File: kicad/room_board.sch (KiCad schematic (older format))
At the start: 22 parts, among them K1 CONN_3, U1 MSP430G2553IN20, U2 7805, U3 DHT

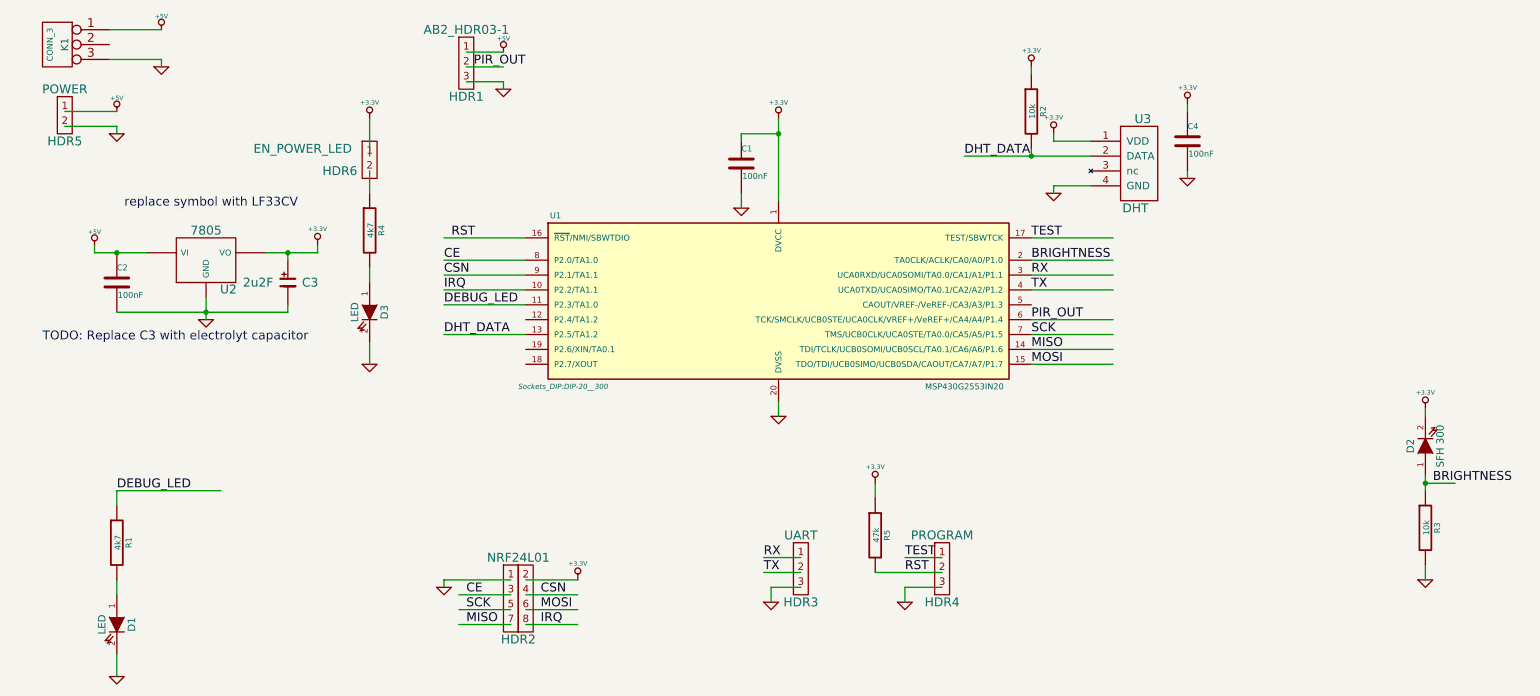
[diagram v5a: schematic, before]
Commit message: update schematic/layout
- replace LM7805 symbol with LM33CV in schematic and layout
- add 3.3V power connector in schematic and layout
- replace 3pin uart with 6pin. only in schematic not done yet in layout
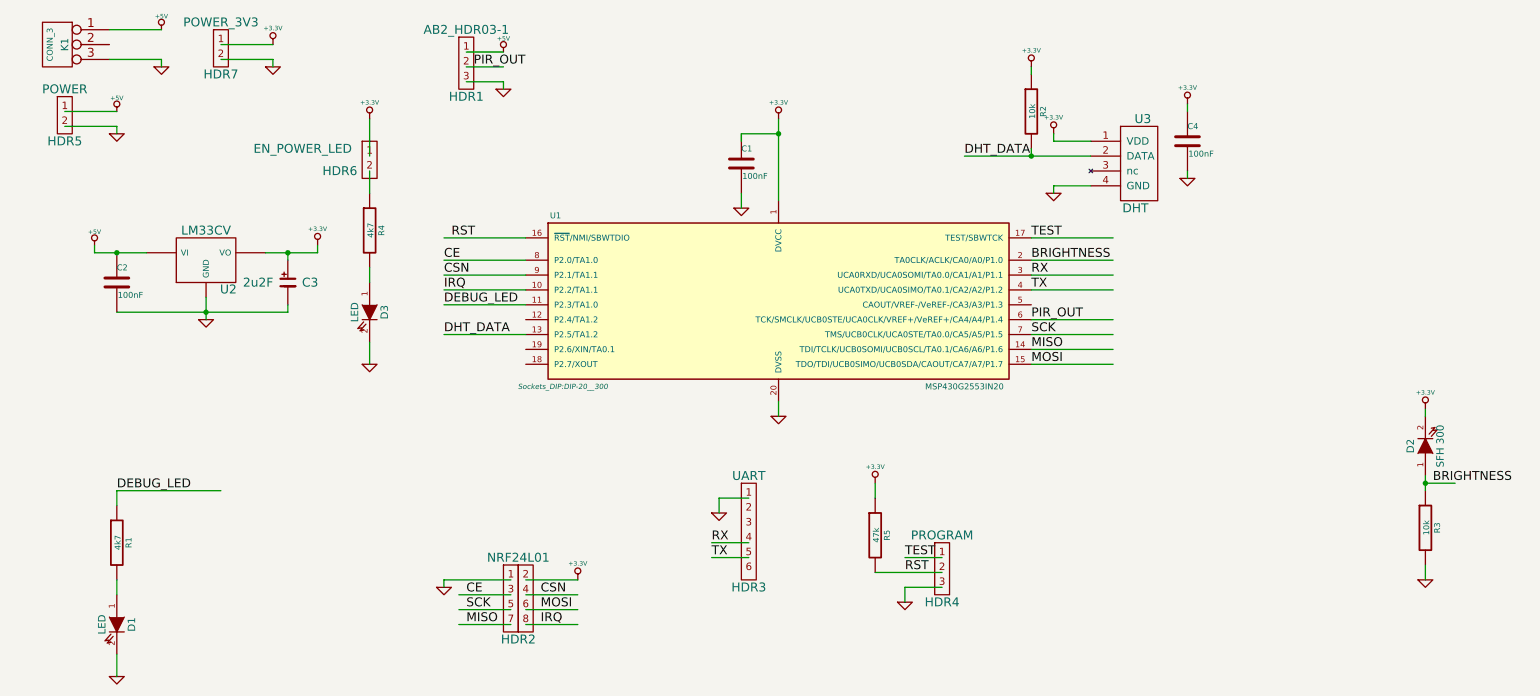
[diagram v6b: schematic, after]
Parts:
- removed HDR3: UART, ab2_header:AB2_HDR_M03-1V, symbol AB2_HDR03-1
- removed U2: 7805, Discret:LM78XXV, symbol 7805
- added HDR3: UART, ab2_header:AB2_HDR_M06-1H-L, symbol AB2_HDR06-1
- added HDR7: POWER_3V3, ab2_header:AB2_HDR_M02-1V, symbol AB2_HDR02-1
- added U2: LM33CV, Discret:LM78XXV, symbol LM33CV
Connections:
- wire segments 76 -> 79
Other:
- note removed: "TODO: Replace C3 with electrolyt capacitor"
- note removed: "replace symbol with LF33CV"
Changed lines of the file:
@@
 LIBS:ab2_usb
 LIBS:ab2_xtal
+LIBS:fr_regulator
 LIBS:room_board-cache
 EELAYER 25 0
@@
 $EndComp
 $Comp
-L 7805 U2
-U 1 1 541A1855
-P 1750 2250
-F 0 "U2" H 1900 2054 60  0000 C CNN
-F 1 "7805" H 1750 2450 60  0000 C CNN
-F 2 "Discret:LM78XXV" H 1750 2250 60  0001 C CNN
-F 3 "" H 1750 2250 60  0000 C CNN
-	1    1750 2250
-	1    0    0    -1
-$EndComp
-$Comp
 L C C2
 U 1 1 541A1A82
@@
 	1    0    0    -1
 $EndComp
-Text Notes 1200 1900 0    60   ~ 0
-replace symbol with LF33CV
 $Comp
 L AB2_HDR03-1 HDR1
@@
 	3800 4400 3350 4400
 $Comp
-L AB2_HDR03-1 HDR3
-U 1 1 54265497
-P 5750 4250
-F 0 "HDR3" H 5750 3950 60  0000 C CNN
-F 1 "UART" H 5750 4400 60  0000 C CNN
-F 2 "ab2_header:AB2_HDR_M03-1V" H 5750 4250 60  0001 C CNN
-F 3 "" H 5750 4250 60  0000 C CNN
-	1    5750 4250
-	1    0    0    -1
-$EndComp
-$Comp
 L AB2_HDR03-1 HDR4
 U 1 1 542654DE
@@
 	1    0    0    -1
 $EndComp
-Text Label 5500 4250 0    60   ~ 0
+Text Label 5150 4150 0    60   ~ 0
 RX
-Text Label 5500 4350 0    60   ~ 0
+Text Label 5150 4250 0    60   ~ 0
 TX
 $Comp
 L GND #PWR023
 U 1 1 5426577D
-P 5550 4550
-F 0 "#PWR023" H 5550 4550 30  0001 C CNN
-F 1 "GND" H 5550 4480 30  0001 C CNN
-F 2 "" H 5550 4550 60  0000 C CNN
-F 3 "" H 5550 4550 60  0000 C CNN
-	1    5550 4550
-	1    0    0    -1
-$EndComp
-Wire Wire Line
-	5500 4250 5750 4250
-Wire Wire Line
-	5750 4350 5500 4350
-Wire Wire Line
-	5750 4450 5550 4450
-Wire Wire Line
-	5550 4450 5550 4550
+P 5200 3950
+F 0 "#PWR023" H 5200 3950 30  0001 C CNN
+F 1 "GND" H 5200 3880 30  0001 C CNN
+F 2 "" H 5200 3950 60  0000 C CNN
+F 3 "" H 5200 3950 60  0000 C CNN
+	1    5200 3950
+	1    0    0    -1
+$EndComp
+Wire Wire Line
+	5150 4150 5400 4150
+Wire Wire Line
+	5400 4250 5150 4250
+Wire Wire Line
+	5400 3850 5200 3850
+Wire Wire Line
+	5200 3850 5200 3950
 Wire Wire Line
 	6700 4250 6450 4250
@@
 Wire Wire Line
 	5350 1800 5350 1900
-Text Notes 650  2800 0    60   ~ 0
-TODO: Replace C3 with electrolyt capacitor
 $Comp
 L AB2_HDR02-1 HDR6
@@
 Wire Wire Line
 	2300 2600 2300 2550
+$Comp
+L LM33CV U2
+U 1 1 54861353
+P 1750 2250
+F 0 "U2" H 1900 2054 60  0000 C CNN
+F 1 "LM33CV" H 1750 2450 60  0000 C CNN
+F 2 "Discret:LM78XXV" H 1750 2250 60  0001 C CNN
+F 3 "" H 1750 2250 60  0000 C CNN
+	1    1750 2250
+	1    0    0    -1
+$EndComp
+$Comp
+L AB2_HDR02-1 HDR7
+U 1 1 54864496
+P 1850 800
+F 0 "HDR7" H 1850 600 60  0000 C CNN
+F 1 "POWER_3V3" H 1850 950 60  0000 C CNN
+F 2 "ab2_header:AB2_HDR_M02-1V" H 1850 800 60  0001 C CNN
+F 3 "" H 1850 800 60  0000 C CNN
+	1    1850 800
+	1    0    0    -1
+$EndComp
+$Comp
+L GND #PWR028
+U 1 1 5486449C
+P 2200 950
+F 0 "#PWR028" H 2200 950 30  0001 C CNN
+F 1 "GND" H 2200 880 30  0001 C CNN
+F 2 "" H 2200 950 60  0000 C CNN
+F 3 "" H 2200 950 60  0000 C CNN
+	1    2200 950
+	1    0    0    -1
+$EndComp
+Wire Wire Line
+	1850 900  2200 900
+Wire Wire Line
+	2200 900  2200 950
+Wire Wire Line
+	2200 800  1850 800
+$Comp
+L +3.3V #PWR029
+U 1 1 5486460A
+P 2200 800
+F 0 "#PWR029" H 2200 760 30  0001 C CNN
+F 1 "+3.3V" H 2200 910 30  0000 C CNN
+F 2 "" H 2200 800 60  0000 C CNN
+F 3 "" H 2200 800 60  0000 C CNN
+	1    2200 800
+	1    0    0    -1
+$EndComp
+$Comp
+L AB2_HDR06-1 HDR3
+U 1 1 54864BD2
+P 5400 3850
+F 0 "HDR3" H 5400 3250 60  0000 C CNN
+F 1 "UART" H 5400 4000 60  0000 C CNN
+F 2 "ab2_header:AB2_HDR_M06-1H-L" H 5400 3850 60  0001 C CNN
+F 3 "" H 5400 3850 60  0000 C CNN
+	1    5400 3850
+	1    0    0    -1
+$EndComp
 $EndSCHEMATC

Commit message: fix layout of uart connector
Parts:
- HDR3: footprint ab2_header:AB2_HDR_M06-1H-L -> ab2_header:AB2_HDR_M06-1V
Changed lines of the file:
@@
 F 0 "HDR3" H 5400 3250 60  0000 C CNN
 F 1 "UART" H 5400 4000 60  0000 C CNN
-F 2 "ab2_header:AB2_HDR_M06-1H-L" H 5400 3850 60  0001 C CNN
+F 2 "ab2_header:AB2_HDR_M06-1V" H 5400 3850 60  0001 C CNN
 F 3 "" H 5400 3850 60  0000 C CNN
 	1    5400 3850
